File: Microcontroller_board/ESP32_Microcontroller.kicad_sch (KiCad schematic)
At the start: 10 parts, among them SW1 Reset, U1 ESP32-WROOM-E

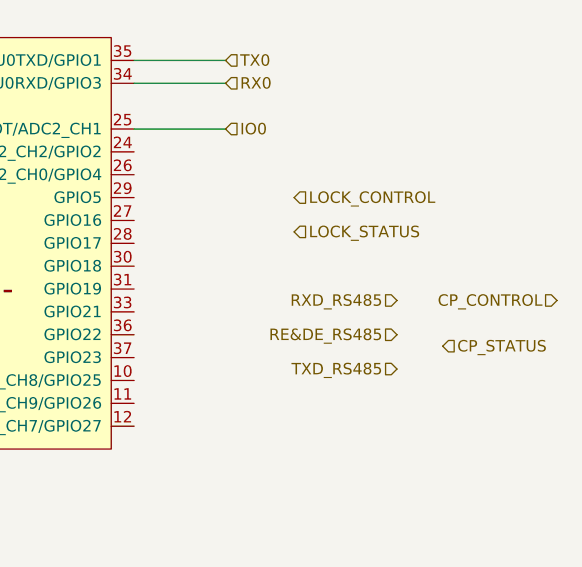
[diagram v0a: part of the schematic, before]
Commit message: Delete sensingboard project and add stm32 micro to the schematic
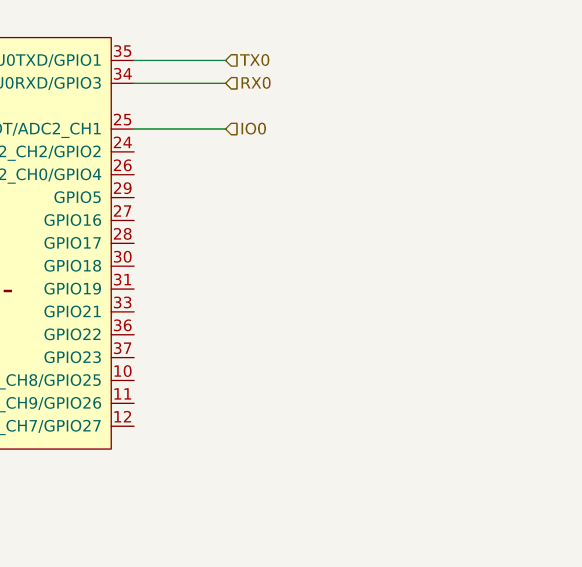
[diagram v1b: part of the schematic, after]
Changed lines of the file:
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@@
-    (effects (font (size 1.27 1.27)) (justify right))
-  )
-  (hierarchical_label "TXD_RS485" (shape input) (at 208.28 127 180) (fields_autoplaced)
     (effects (font (size 1.27 1.27)) (justify right))
   )
   (hierarchical_label "RX0" (shape input) (at 189.23 95.25 0) (fields_autoplaced)
     (effects (font (size 1.27 1.27)) (justify left))
-  )
-  (hierarchical_label "LOCK_STATUS" (shape input) (at 196.85 111.76 0) (fields_autoplaced)
-    (effects (font (size 1.27 1.27)) (justify left))
-  )
-  (hierarchical_label "RE&DE_RS485" (shape input) (at 208.28 123.19 180) (fields_autoplaced)
-    (effects (font (size 1.27 1.27)) (justify right))
   )
   (hierarchical_label "EN" (shape input) (at 82.55 92.71 180) (fields_autoplaced)
@@
     (effects (font (size 1.27 1.27)) (justify left))
   )
-  (hierarchical_label "RXD_RS485" (shape input) (at 208.28 119.38 180) (fields_autoplaced)
-    (effects (font (size 1.27 1.27)) (justify right))
-  )
-  (hierarchical_label "CP_CONTROL" (shape input) (at 226.06 119.38 180) (fields_autoplaced)
-    (effects (font (size 1.27 1.27)) (justify right))
-  )
-  (hierarchical_label "CP_STATUS" (shape input) (at 213.36 124.46 0) (fields_autoplaced)
-    (effects (font (size 1.27 1.27)) (justify left))
-  )
-  (hierarchical_label "LOCK_CONTROL" (shape input) (at 196.85 107.95 0) (fields_autoplaced)
-    (effects (font (size 1.27 1.27)) (justify left))
-  )
